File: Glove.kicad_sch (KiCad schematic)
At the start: 36 parts, among them J1 USB_C_Receptacle_USB2.0, J2 Joystick, Q1 2N7002, Q2 2N7002, U1 LM1117-3.3, U2 ESP32-WROOM-32D, U3 CP2102N-Axx-xQFN24

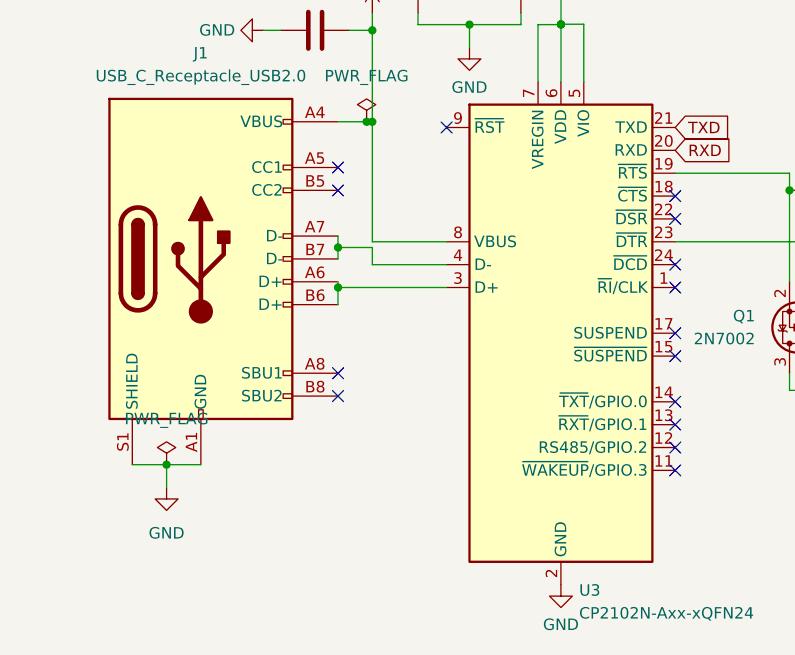
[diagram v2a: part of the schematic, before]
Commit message: Add 5.1k Pulldown for CC1 and CC2
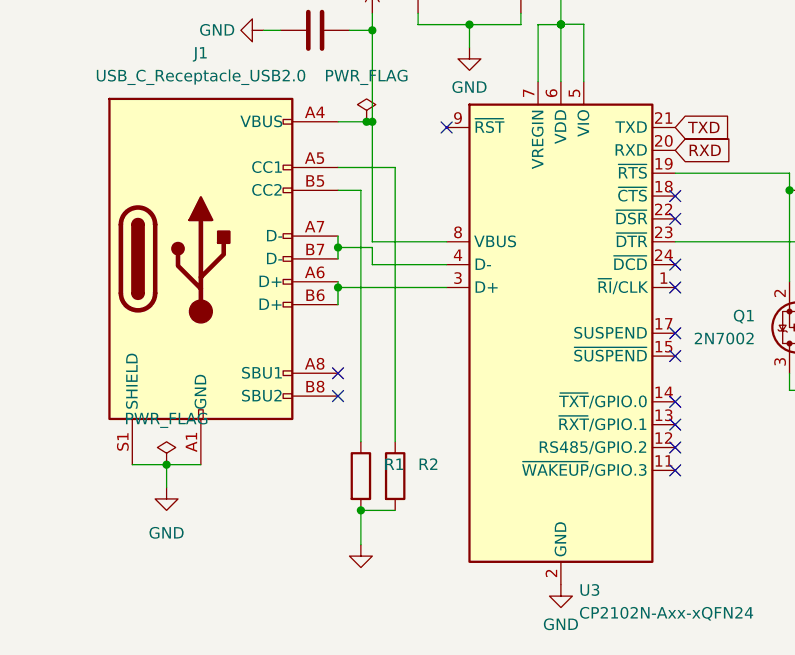
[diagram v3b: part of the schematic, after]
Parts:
- added R1, R2: (no value), symbol Device:R
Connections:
- net GND: now also R1.2, R2.2
- net at J1.A5 (CC1): now also R2.1
- net at J1.B5 (CC2): now also R1.1
- no-connect marks 25 -> 23
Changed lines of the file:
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@@
   (junction (at 60.325 126.365) (diameter 0) (color 0 0 0 0)
+  )
+  (junction (at 48.26 180.34) (diameter 0) (color 0 0 0 0)
   )
   (junction (at 70.485 126.3242) (diameter 0) (color 0 0 0 0)
@@
   (no_connect (at 102.87 85.09))
   (no_connect (at 57.785 137.795))
-  (no_connect (at 45.72 144.78))
   (no_connect (at 102.87 80.01))
   (no_connect (at 83.185 163.195))
@@
   (no_connect (at 45.72 167.64))
   (no_connect (at 83.185 145.415))
-  (no_connect (at 45.72 142.24))
   (no_connect (at 83.185 153.035))
   (no_connect (at 83.185 170.815))
@@
     (stroke (width 0) (type default) (color 0 0 0 0))
   )
+  (wire (pts (xy 52.07 142.24) (xy 52.07 172.72))
+    (stroke (width 0) (type default) (color 0 0 0 0))
+  )
   (wire (pts (xy 39.37 21.59) (xy 44.45 21.59))
     (stroke (width 0) (type default) (color 0 0 0 0))
   )
+  (wire (pts (xy 48.26 180.34) (xy 52.07 180.34))
+    (stroke (width 0) (type default) (color 0 0 0 0))
+  )
   (wire (pts (xy 31.75 29.21) (xy 31.75 35.56))
     (stroke (width 0) (type default) (color 0 0 0 0))
@@
     (stroke (width 0) (type default) (color 0 0 0 0))
   )
+  (wire (pts (xy 45.72 142.24) (xy 52.07 142.24))
+    (stroke (width 0) (type default) (color 0 0 0 0))
+  )
   (wire (pts (xy 194.31 90.17) (xy 187.96 90.17))
     (stroke (width 0) (type default) (color 0 0 0 0))
@@
     (stroke (width 0) (type default) (color 0 0 0 0))
   )
+  (wire (pts (xy 48.26 144.78) (xy 48.26 172.72))
+    (stroke (width 0) (type default) (color 0 0 0 0))
+  )
   (wire (pts (xy 238.125 121.285) (xy 235.585 121.285))
     (stroke (width 0) (type default) (color 0 0 0 0))
@@
     (stroke (width 0) (type default) (color 0 0 0 0))
   )
+  (wire (pts (xy 48.26 180.34) (xy 48.26 184.15))
+    (stroke (width 0) (type default) (color 0 0 0 0))
+  )
   (wire (pts (xy 118.11 29.21) (xy 125.73 29.21))
     (stroke (width 0) (type default) (color 0 0 0 0))
@@
   )
   (wire (pts (xy 235.585 121.285) (xy 235.585 123.825))
+    (stroke (width 0) (type default) (color 0 0 0 0))
+  )
+  (wire (pts (xy 45.72 144.78) (xy 48.26 144.78))
     (stroke (width 0) (type default) (color 0 0 0 0))
   )
@@
     (pin "3")
   )
+  (symbol (lib_id "power:GND") (at 48.26 184.15 0) (unit 1)
+    (in_bom yes) (on_board yes) (fields_autoplaced)
+    (property "Reference" "#PWR021" (id 0) (at 48.26 190.5 0)
+      (effects (font (size 1.27 1.27)) hide)
+    )
+    (property "Value" "" (id 1) (at 48.26 189.23 0))
+    (property "Footprint" "" (id 2) (at 48.26 184.15 0)
+      (effects (font (size 1.27 1.27)) hide)
+    )
+    (property "Datasheet" "" (id 3) (at 48.26 184.15 0)
+      (effects (font (size 1.27 1.27)) hide)
+    )
+    (pin "1")
+  )
+  (symbol (lib_id "Device:R") (at 48.26 176.53 0) (unit 1)
+    (in_bom yes) (on_board yes) (fields_autoplaced)
+    (property "Reference" "R1" (id 0) (at 50.8 175.2599 0)
+      (effects (font (size 1.27 1.27)) (justify left))
+    )
+    (property "Value" "" (id 1) (at 50.8 177.7999 0)
+      (effects (font (size 1.27 1.27)) (justify left))
+    )
+    (property "Footprint" "" (id 2) (at 46.482 176.53 90)
+      (effects (font (size 1.27 1.27)) hide)
+    )
+    (property "Datasheet" "~" (id 3) (at 48.26 176.53 0)
+      (effects (font (size 1.27 1.27)) hide)
+    )
+    (pin "1")
+    (pin "2")
+  )
   (symbol (lib_id "Device:R") (at 146.05 125.73 90) (unit 1)
     (in_bom yes) (on_board yes) (fields_autoplaced)
@@
     (pin "1")
   )
+  (symbol (lib_id "Device:R") (at 52.07 176.53 0) (unit 1)
+    (in_bom yes) (on_board yes) (fields_autoplaced)
+    (property "Reference" "R2" (id 0) (at 54.61 175.2599 0)
+      (effects (font (size 1.27 1.27)) (justify left))
+    )
+    (property "Value" "" (id 1) (at 54.61 177.7999 0)
+      (effects (font (size 1.27 1.27)) (justify left))
+    )
+    (property "Footprint" "" (id 2) (at 50.292 176.53 90)
+      (effects (font (size 1.27 1.27)) hide)
+    )
+    (property "Datasheet" "~" (id 3) (at 52.07 176.53 0)
+      (effects (font (size 1.27 1.27)) hide)
+    )
+    (pin "1")
+    (pin "2")
+  )
   (symbol (lib_id "power:+5V") (at 187.96 46.99 0) (unit 1)
     (in_bom yes) (on_board yes) (fields_autoplaced)
@@
       (reference "#PWR020") (unit 1) (value "GND") (footprint "")
     )
+    (path "/295a80a6-aa44-486d-a65a-1011ad36c7a1"
+      (reference "#PWR021") (unit 1) (value "GND") (footprint "")
+    )
     (path "/aebefabf-3e70-45e5-94ab-817eaaf9a010"
       (reference "BTN_A1") (unit 1) (value "Button A") (footprint "Connector_JST:JST_XH_B2B-XH-A_1x02_P2.50mm_Vertical")
@@
       (reference "Q2") (unit 1) (value "2N7002") (footprint "Package_TO_SOT_SMD:SOT-23")
     )
+    (path "/3109af89-69b9-40ec-aa8b-2a099f0472f9"
+      (reference "R1") (unit 1) (value "5.1k") (footprint "Resistor_SMD:R_0805_2012Metric_Pad1.20x1.40mm_HandSolder")
+    )
+    (path "/b3f63285-4de9-426f-81ae-178a99ee1972"
+      (reference "R2") (unit 1) (value "5.1k") (footprint "Resistor_SMD:R_0805_2012Metric_Pad1.20x1.40mm_HandSolder")
+    )
     (path "/9ef604ba-2d90-4fa2-9442-62b9a66ead0e"

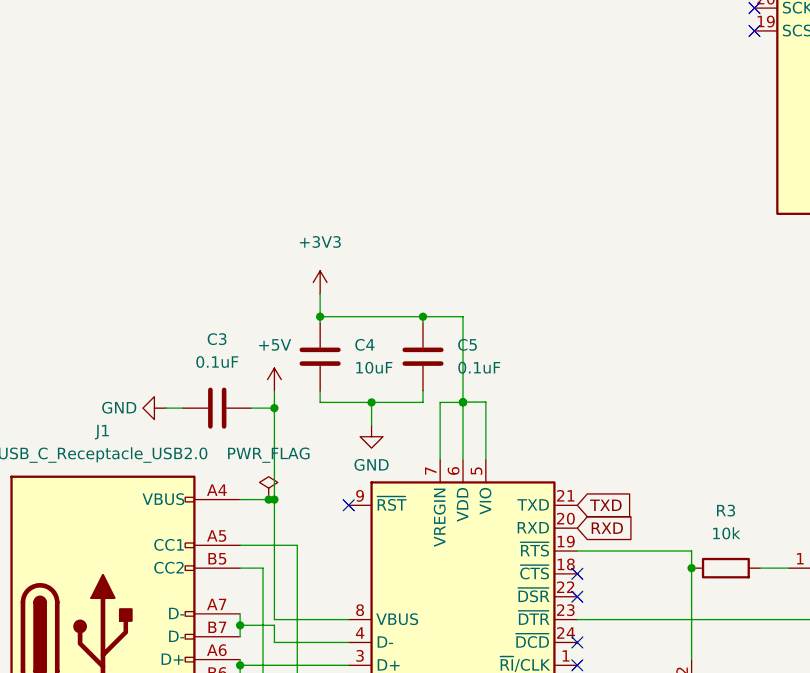
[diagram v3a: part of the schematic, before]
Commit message: Remove in-pad vias and add 1k pullup for CP2102 RST
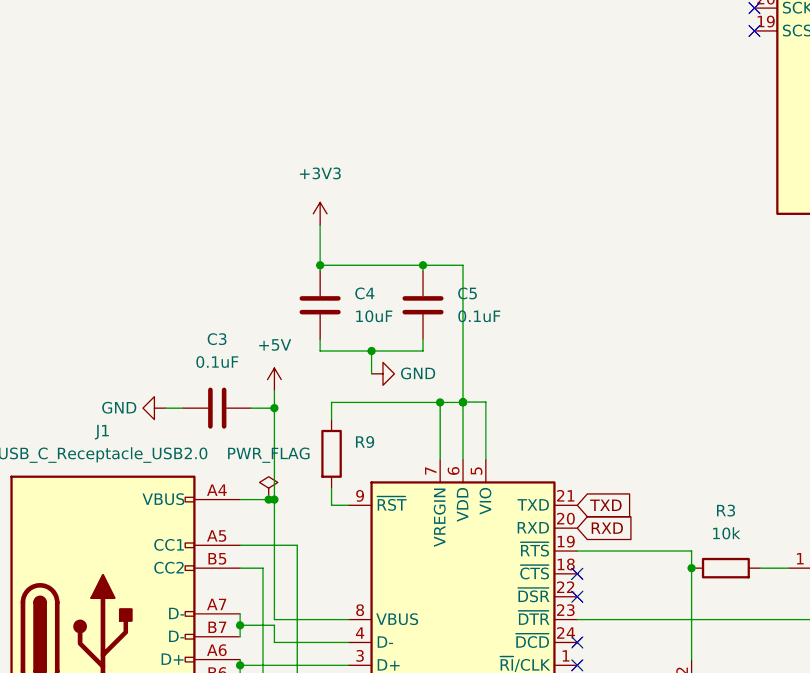
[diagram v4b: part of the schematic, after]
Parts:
- added R9: (no value), symbol Device:R
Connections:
- net +3V3: now also R9.1
- net at U3.9 (~{RST}): now also R9.2
- no-connect marks 23 -> 22
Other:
- moved on the sheet: C4, C5

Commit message: Move decoupling capacitors
Signed-off-by: Kozova1 <mug66kk@gmail.com>
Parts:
- C_Out1: value 100uF -> (none)
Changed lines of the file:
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@@
       (effects (font (size 1.27 1.27)) (justify left))
     )
-    (property "Value" "100uF" (id 1) (at 48.26 28.3209 0)
+    (property "Value" "" (id 1) (at 48.26 28.3209 0)
       (effects (font (size 1.27 1.27)) (justify left))
     )
@@
     )
     (path "/f14a48c2-89dc-41e5-ba92-ed2063c6246f"
-      (reference "C_Out1") (unit 1) (value "100uF") (footprint "Capacitor_SMD:C_0805_2012Metric_Pad1.18x1.45mm_HandSolder")
+      (reference "C_Out1") (unit 1) (value "10uF") (footprint "Capacitor_SMD:C_0805_2012Metric_Pad1.18x1.45mm_HandSolder")
     )
     (path "/b24d4a6b-032c-44bd-924b-dd7f40676b34"

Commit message: Route D- and D+ as differential pair
Signed-off-by: David Vogman <davidv@edgegaming.gg>
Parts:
- C_Out1: value (none) -> 10uF
- R1, R2: value (none) -> 5.1k; footprint (none) -> Resistor_SMD:R_0805_2012Metric_Pad1.20x1.40mm_HandSolder
- R9: value (none) -> 1k; footprint (none) -> Resistor_SMD:R_0805_2012Metric_Pad1.20x1.40mm_HandSolder
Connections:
- net D+: now reaches J1.A6 (D+), J1.B6 (D+), U3.3 (D+)
- net D-: now reaches J1.A7 (D-), J1.B7 (D-), U3.4 (D-)
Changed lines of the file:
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@@
+    (effects (font (size 1.27 1.27)) (justify left bottom))
+  )
+  (label "D+" (at 53.8515 155.575 0)
     (effects (font (size 1.27 1.27)) (justify left bottom))
   )
@@
   )
   (label "MTCK" (at 150.495 130.81 0)
+    (effects (font (size 1.27 1.27)) (justify left bottom))
+  )
+  (label "D-" (at 54.0743 153.035 0)
     (effects (font (size 1.27 1.27)) (justify left bottom))
   )
@@
       (effects (font (size 1.27 1.27)) (justify left))
     )
-    (property "Value" "" (id 1) (at 58.42 133.3499 0)
-      (effects (font (size 1.27 1.27)) (justify left))
-    )
-    (property "Footprint" "" (id 2) (at 54.102 132.08 90)
+    (property "Value" "1k" (id 1) (at 58.42 133.3499 0)
+      (effects (font (size 1.27 1.27)) (justify left))
+    )
+    (property "Footprint" "Resistor_SMD:R_0805_2012Metric_Pad1.20x1.40mm_HandSolder" (id 2) (at 54.102 132.08 90)
       (effects (font (size 1.27 1.27)) hide)
     )
@@
       (effects (font (size 1.27 1.27)) hide)
     )
-    (property "Value" "" (id 1) (at 48.26 189.23 0))
+    (property "Value" "GND" (id 1) (at 48.26 189.23 0))
     (property "Footprint" "" (id 2) (at 48.26 184.15 0)
       (effects (font (size 1.27 1.27)) hide)
@@
       (effects (font (size 1.27 1.27)) (justify left))
     )
-    (property "Value" "" (id 1) (at 50.8 177.7999 0)
-      (effects (font (size 1.27 1.27)) (justify left))
-    )
-    (property "Footprint" "" (id 2) (at 46.482 176.53 90)
+    (property "Value" "5.1k" (id 1) (at 50.8 177.7999 0)
+      (effects (font (size 1.27 1.27)) (justify left))
+    )
+    (property "Footprint" "Resistor_SMD:R_0805_2012Metric_Pad1.20x1.40mm_HandSolder" (id 2) (at 46.482 176.53 90)
       (effects (font (size 1.27 1.27)) hide)
     )
@@
       (effects (font (size 1.27 1.27)) (justify left))
     )
-    (property "Value" "" (id 1) (at 54.61 177.7999 0)
-      (effects (font (size 1.27 1.27)) (justify left))
-    )
-    (property "Footprint" "" (id 2) (at 50.292 176.53 90)
+    (property "Value" "5.1k" (id 1) (at 54.61 177.7999 0)
+      (effects (font (size 1.27 1.27)) (justify left))
+    )
+    (property "Footprint" "Resistor_SMD:R_0805_2012Metric_Pad1.20x1.40mm_HandSolder" (id 2) (at 50.292 176.53 90)
       (effects (font (size 1.27 1.27)) hide)
     )
@@
       (effects (font (size 1.27 1.27)) (justify left))
     )
-    (property "Value" "" (id 1) (at 48.26 28.3209 0)
-      (effects (font (size 1.27 1.27)) (justify left))
-    )
+    (property "Value" "10uF" (id 1) (at 48.26 28.3209 0)
+      (effects (font (size 1.27 1.27)) (justify left))
+    )

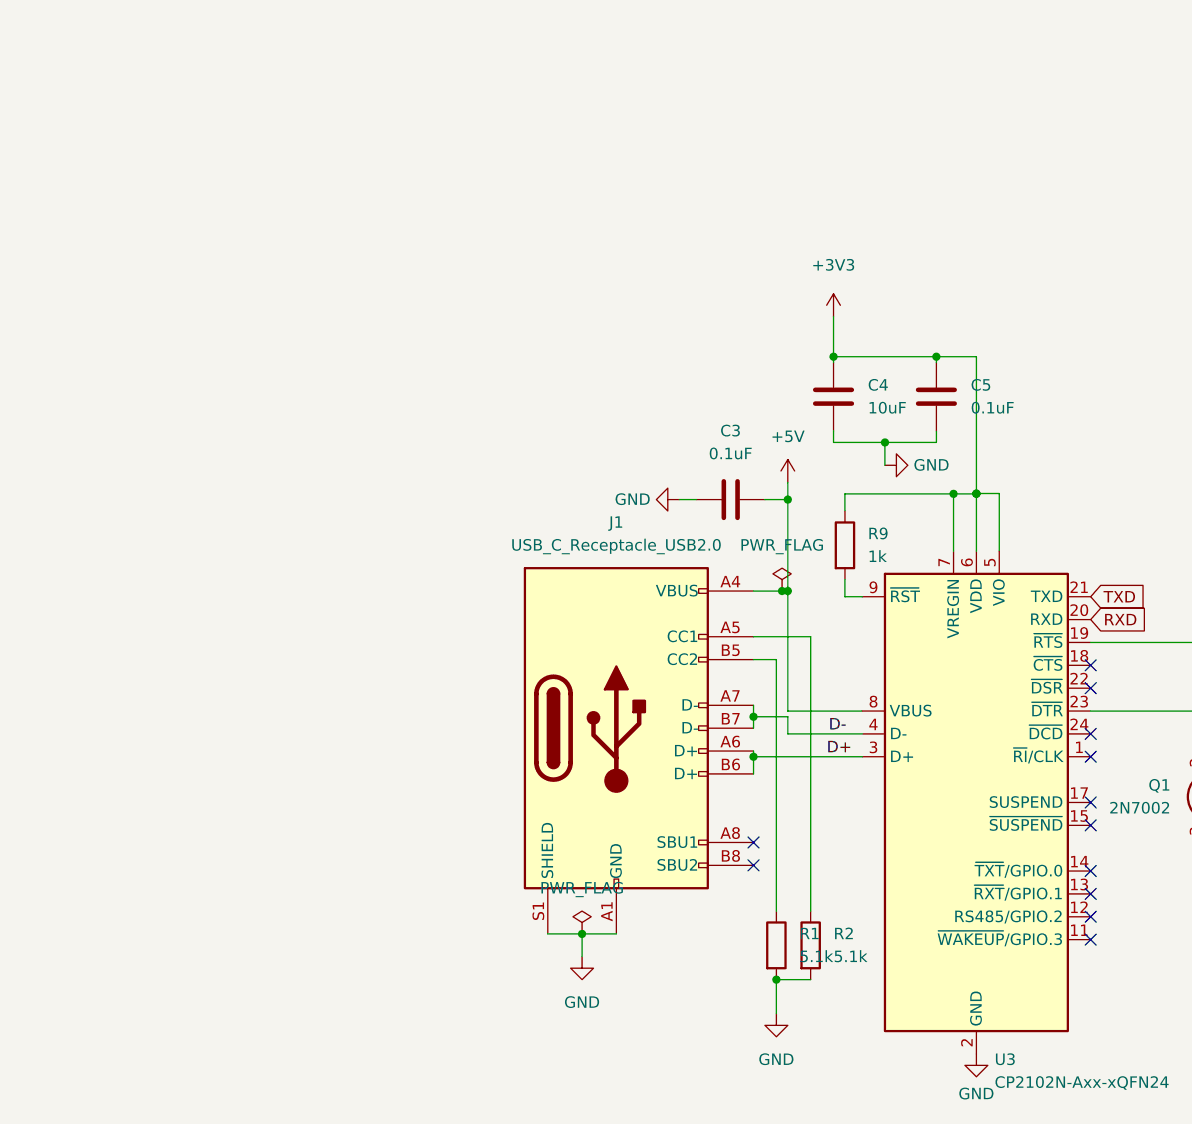
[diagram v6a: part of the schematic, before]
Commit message: Fix routing, move capacitors closer to ICs
Signed-off-by: Kozova1 <mug66kk@gmail.com>
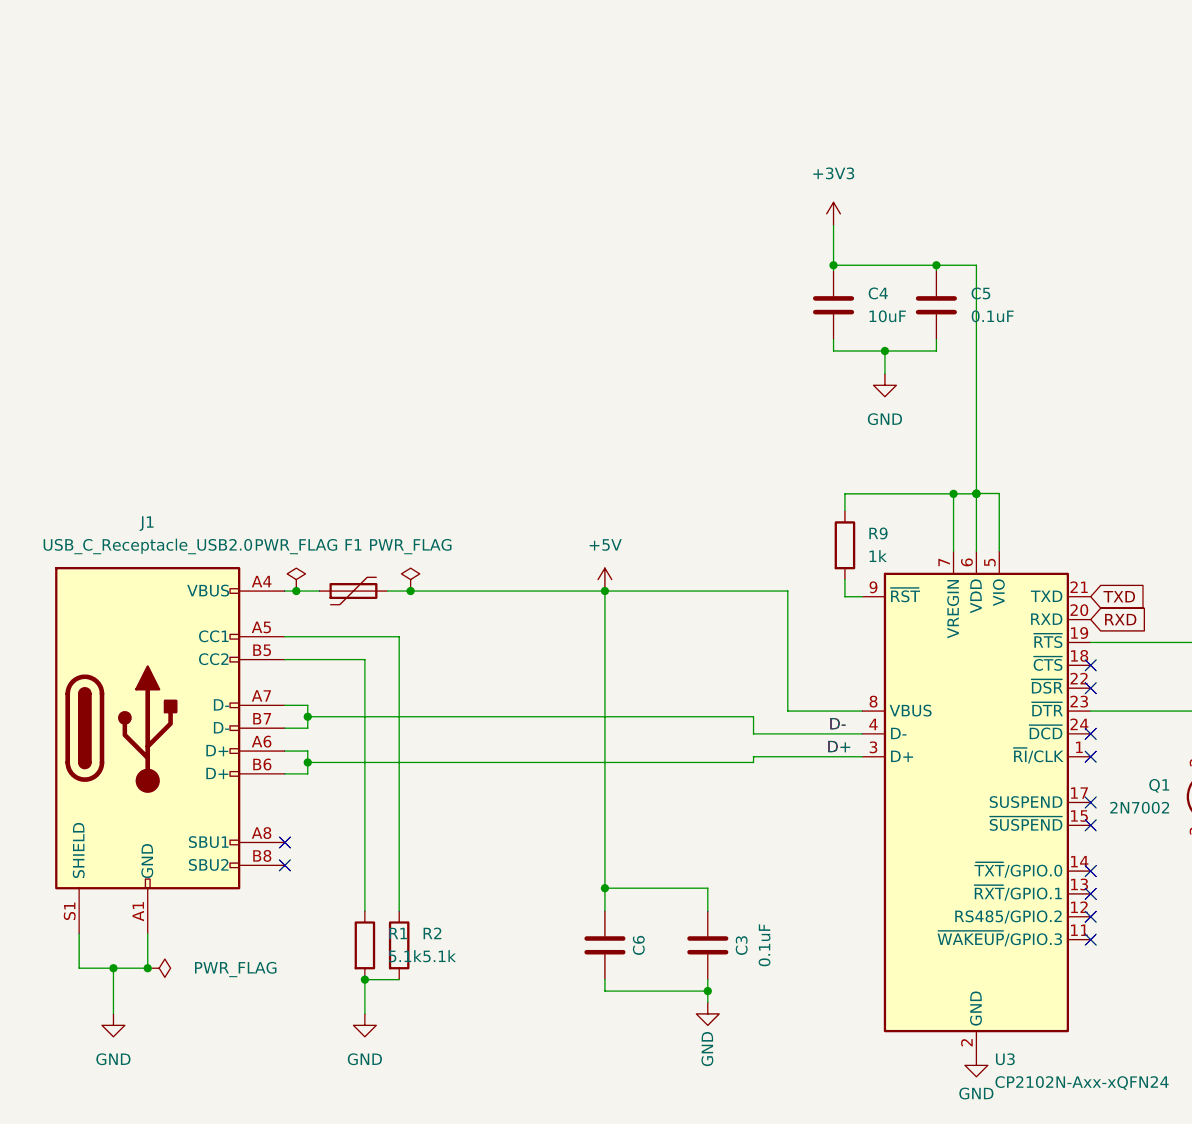
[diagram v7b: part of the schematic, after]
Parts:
- added C6: (no value), symbol Device:C
- added F1: (no value), symbol Device:Polyfuse
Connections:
- net +5V: now also C6.2, F1.2; no longer J1.A4 (VBUS), J1.A9 (VBUS), J1.B4 (VBUS), J1.B9 (VBUS)
- net GND: now also C6.1
- new net: F1.1, J1.A4 (VBUS), J1.A9 (VBUS), J1.B4 (VBUS), J1.B9 (VBUS)
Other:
- moved on the sheet: C3, C4, C5, J1, R1, R2
